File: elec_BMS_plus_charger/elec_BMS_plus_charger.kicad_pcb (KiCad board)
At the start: 2 copper layers, 94 x 41 mm, 51 parts, among them J1 JST EH 2, J13 Dynamixel-3, J14 Dynamixel-3, J2 JST SH, J7 JST SH, Q1 BSZ034N04LS, Q2 BSZ034N04LS, U1 HY2120, U2 BQ25887RGE

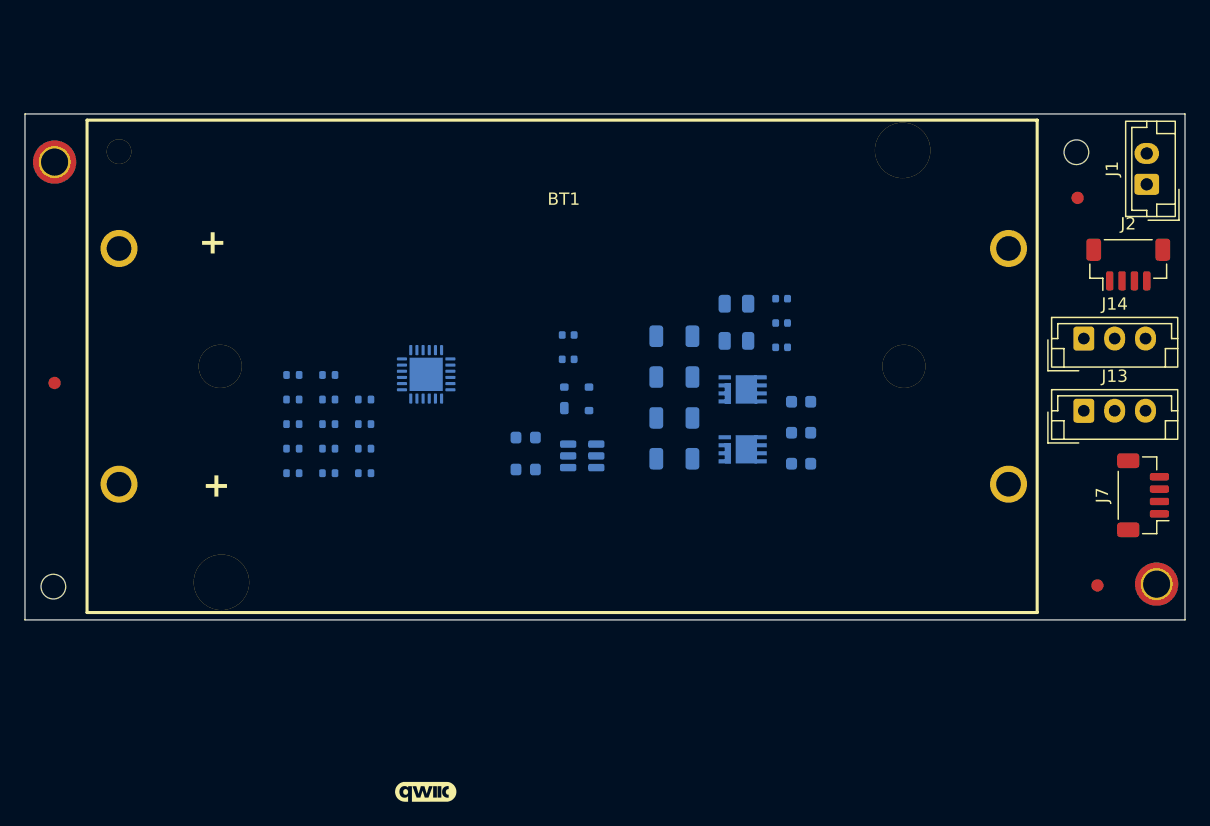
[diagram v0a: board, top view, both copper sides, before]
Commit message: [update] Mechanical adaptations.
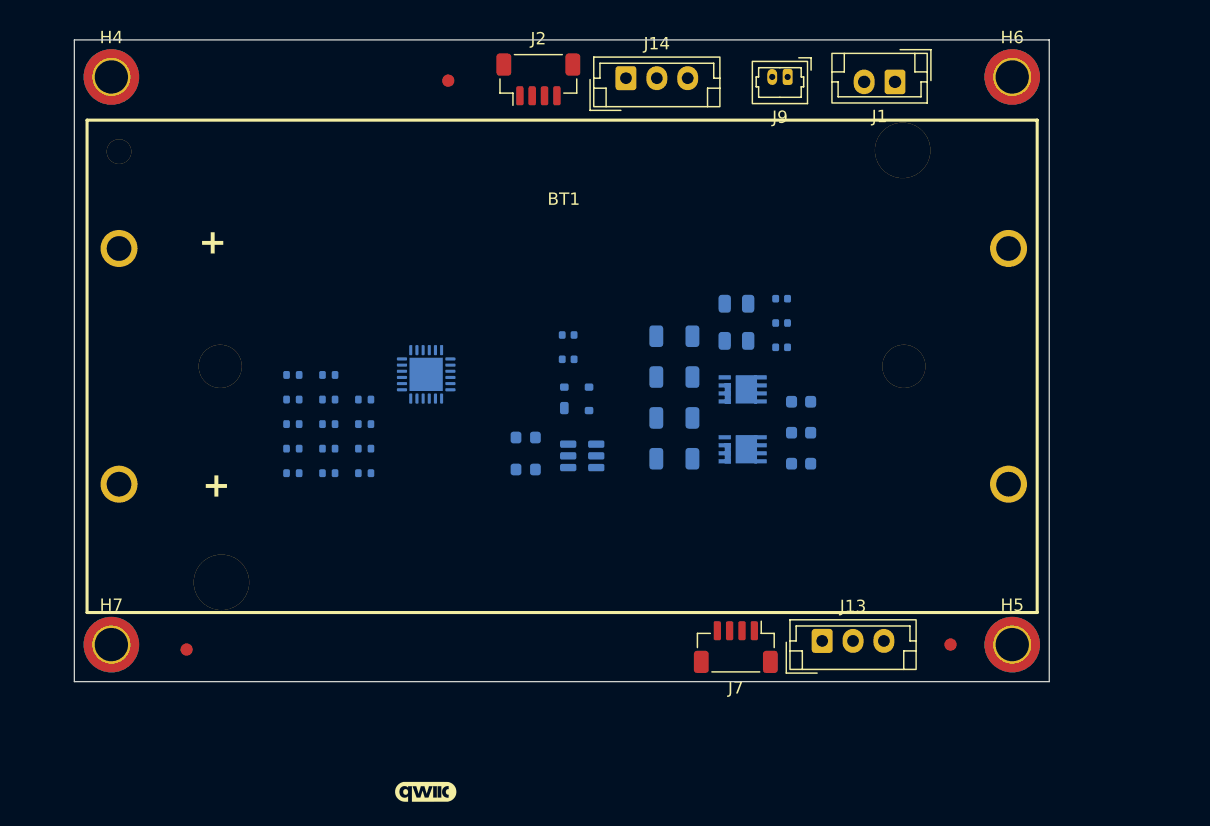
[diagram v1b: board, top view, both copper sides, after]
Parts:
- added J9: Pico2, Connector_Molex:Molex_PicoBlade_53047-0210_1x02_P1.25mm_Vertical, F.Cu at (163.7, 51.6)
- H4, H5: value Mounting Holes M2 -> Mounting Holes M2,5; footprint MountingHole:MountingHole_2.2mm_M2_ISO7380_Pad_TopBottom -> MountingHole:MountingHole_2.7mm_M2.5_ISO7380_Pad_TopBottom
- H6, H7: value Centering Hole 2 mm -> Mounting Holes M2,5; footprint Library_Pollen:MountingHole_2.0mm -> MountingHole:MountingHole_2.7mm_M2.5_ISO7380_Pad_TopBottom
- moved H6 88.0 mm to (181.9, 51.6)
- moved H7 87.8 mm to (108.9, 97.6)
- moved FID2 51.9 mm to (136.2, 51.9)
- moved J2 50.1 mm to (143.5, 51.8)
- moved J14 42.7 mm to (150.6, 51.7)
- moved J7 35.2 mm to (159.5, 97.8), turned to 180 degrees
- moved J13 28.2 mm to (166.5, 97.3)
- moved FID1 24.1 mm to (115.0, 98.0)
- moved J1 22.0 mm to (172.4, 52.0), turned to 180 degrees
- moved FID3 12.8 mm to (176.9, 97.6)
- moved H5 12.7 mm to (181.9, 97.6)
- moved H4 8.29 mm to (108.9, 51.6)
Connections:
- C1 pad 2: Net-(U1-Vss) -> Net-(Q1-S)
- C2 pad 2: Net-(U1-Vss) -> Net-(Q1-S)
- U1 pad 6: Net-(U1-Vss) -> Net-(Q1-S)
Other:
- board size 94 x 41 mm -> 79 x 52 mm

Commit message: [update] BMS+charger DRC OK
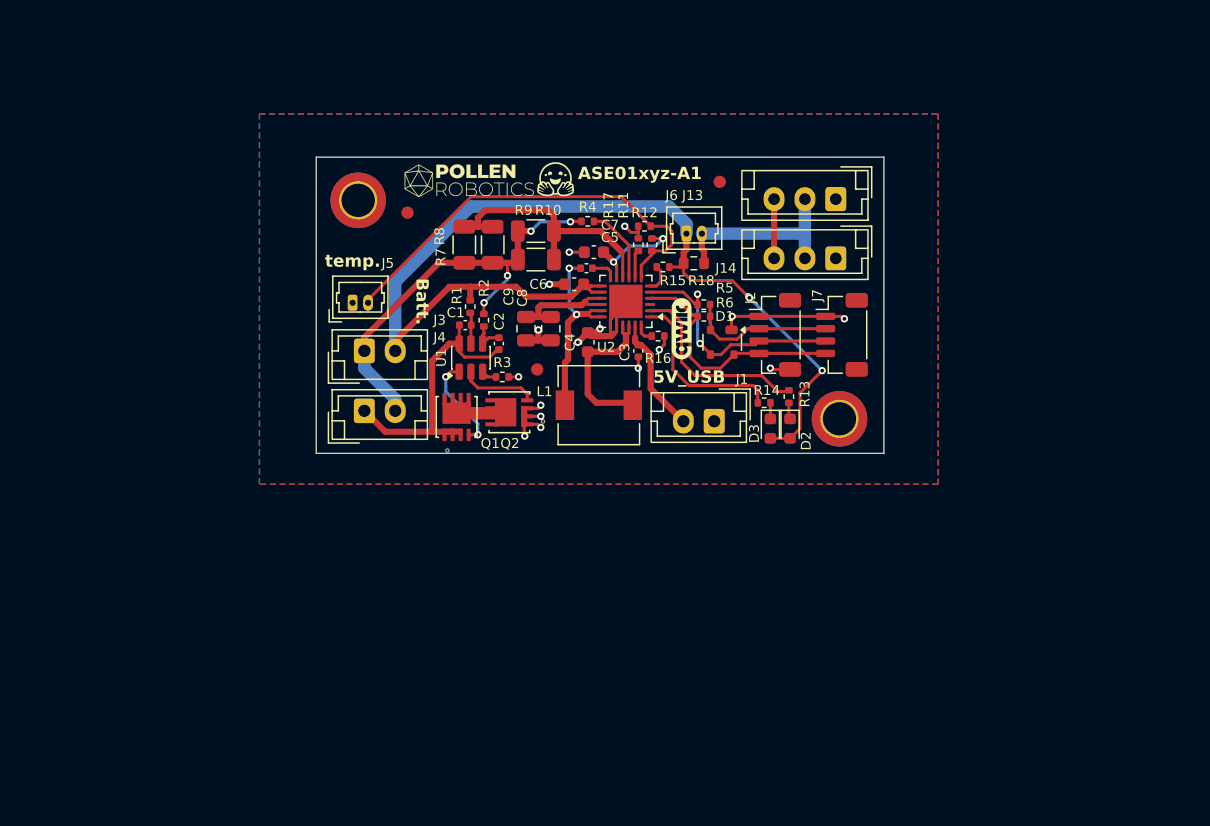
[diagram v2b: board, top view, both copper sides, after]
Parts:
- removed BT1: BH-18650-A1BJ021, LCSC_parts_lib:BAT-TH_L77.0-W39.9_BH-18650-A1BJ021
- removed H6, H7: Mounting Holes M2,5, MountingHole:MountingHole_2.7mm_M2.5_ISO7380_Pad_TopBottom
- removed J9: Pico2, Connector_Molex:Molex_PicoBlade_53047-0210_1x02_P1.25mm_Vertical
- removed TH1: 10k, Resistor_SMD:R_0402_1005Metric
- added J3: JST -EH 2, Connector_JST:JST_EH_B2B-EH-A_1x02_P2.50mm_Vertical, F.Cu at (129.4, 73.8)
- added J4: JST -EH 2, Connector_JST:JST_EH_B2B-EH-A_1x02_P2.50mm_Vertical, F.Cu at (129.4, 78.7)
- added J5: pico2, Library_Pollen:Molex_PicoBlade_53047-0210_1x02_P1.25mm_Vertical, F.Cu at (128.4, 69.9)
- added J6: pico2, Library_Pollen:Molex_PicoBlade_53047-0210_1x02_P1.25mm_Vertical, F.Cu at (155.5, 64.3)
- added R18: 0R, Resistor_SMD:R_0603_1608Metric, F.Cu at (156.1, 66.7)
- C1, C2, C3, C4, C5, C6, C7, C8, C9, D1, D2, D3, H2, H3, Q1, Q2, R1, R10, R11, R12, R13, R14, R15, R16, R17, R2, R3, R4, R5, R6, R7, R8, R9, U1, U2: moved to F.Cu
- J1: value JST EH 2 -> JST -EH 2
- L1: footprint Capacitor_SMD:C_0402_1005Metric -> Inductor_SMD:L_6.3x6.3_H3; moved to F.Cu
- moved G1 42.9 mm to (155.1, 72.0), turned to 90 degrees
- moved FID3 41.9 mm to (158.2, 60.1)
- moved R13 37.3 mm to (163.8, 77.5), turned to 90 degrees
- moved FID1 36.4 mm to (143.4, 75.3)
- moved J13 35.8 mm to (167.6, 61.5), turned to 180 degrees
- moved R14 35.4 mm to (161.8, 78.0), turned to 180 degrees
- moved R5 33.8 mm to (156.9, 70.1), turned to 180 degrees
- moved R6 32.9 mm to (156.9, 71.0), turned to 180 degrees
- moved J1 31.2 mm to (157.7, 79.5)
- moved R11 31.0 mm to (152.7, 65.2), turned to -90 degrees
- moved R12 30.2 mm to (152.1, 63.7), turned to 180 degrees
- moved R15 29.4 mm to (153.6, 67.0)
- moved J2 28.2 mm to (162.7, 72.5), turned to -90 degrees
- moved R4 27.9 mm to (147.5, 63.3)
- moved J7 26.7 mm to (168.1, 72.5), turned to -90 degrees
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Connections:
- J13 pad 2: +BATT -> Net-(J13-Pin_2)
- J14 pad 2: +BATT -> Net-(J13-Pin_2)
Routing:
- net +BATT: track 0.00 -> 83.7 mm, vias 0 -> 2
- net GND: track 0.00 -> 39.2 mm, vias 0 -> 16
- net Net-(J5-Pin_2): track 0.00 -> 34.9 mm
- net /Power/MID: track 0.00 -> 34.8 mm, vias 0 -> 4
- net Net-(J4-Pin_1): track 0.00 -> 22.2 mm
- net Net-(U2-CBSET): track 0.00 -> 21.4 mm
- net Net-(J2-Pin_3): track 0.00 -> 20.2 mm, vias 0 -> 2
- net Net-(J2-Pin_4): track 0.00 -> 19.8 mm
- net Net-(C5-Pad2): track 0.00 -> 16.1 mm, vias 0 -> 2
- net Net-(U2-STAT): track 0.00 -> 15.9 mm
- net Net-(J13-Pin_2): track 0.00 -> 15.6 mm
- net Net-(U2-~{PG}): track 0.00 -> 14.3 mm
- net Net-(C4-Pad1): track 0.00 -> 13.3 mm
- net +3V3: track 0.00 -> 12.1 mm
- net Net-(C8-Pad1): track 0.00 -> 9.63 mm
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- added copper zone on B.Cu, net GND
- added copper zone on F.Cu, net GND
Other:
- board size 79 x 52 mm -> 46 x 24 mm
- board text added: "5V_USB"
- board text added: "ASE01xyz-A1"
- board text added: "Batt."
- board text added: "temp."
